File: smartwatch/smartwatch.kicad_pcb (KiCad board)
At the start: 4 copper layers, 40.1 x 40.1 mm, 33 parts, among them J1 BAT_CON, J2 DC_CON, J3 PROG_INT, J4 Screen, J5 Touch, J6 Power, J8 SD Card, SW1 SW_Push, U1 ESP32-WROVER-E, U2 MCP73831-5-OT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

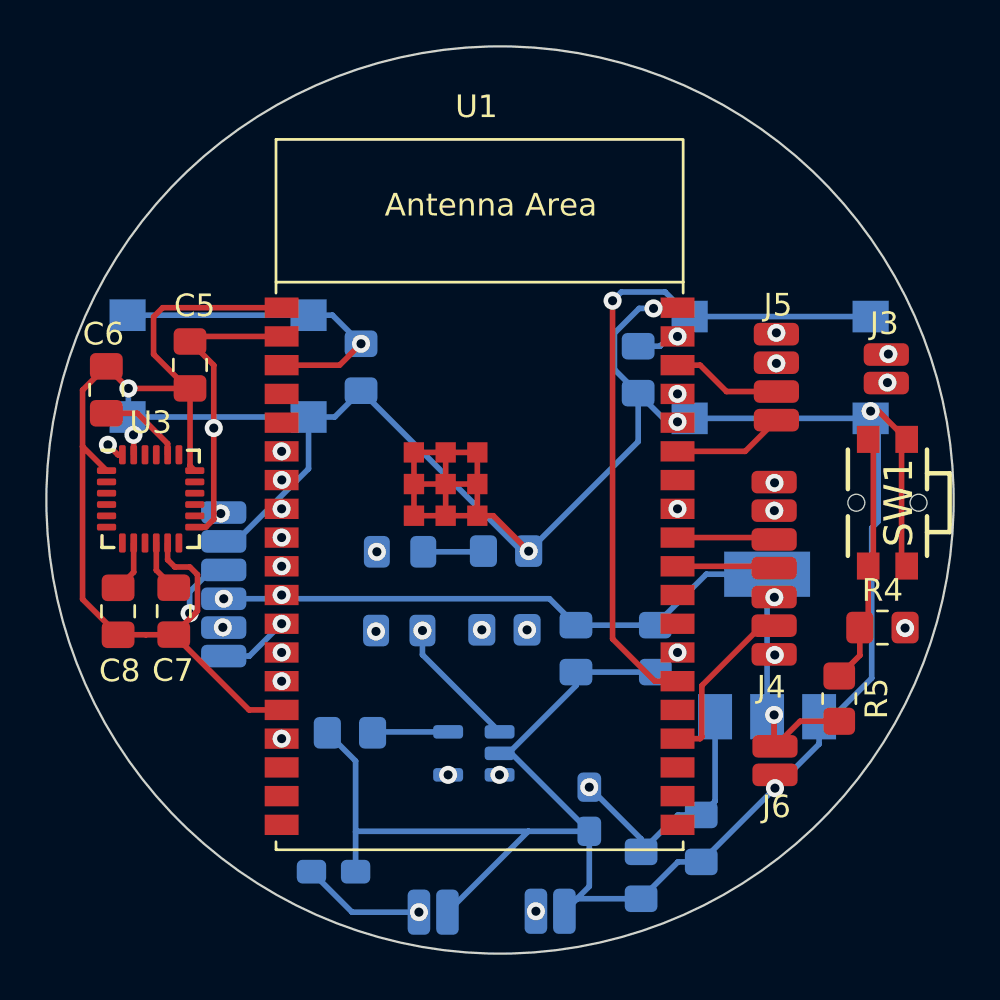
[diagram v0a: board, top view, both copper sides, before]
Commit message: fully redesigned board - ground and power planes :)
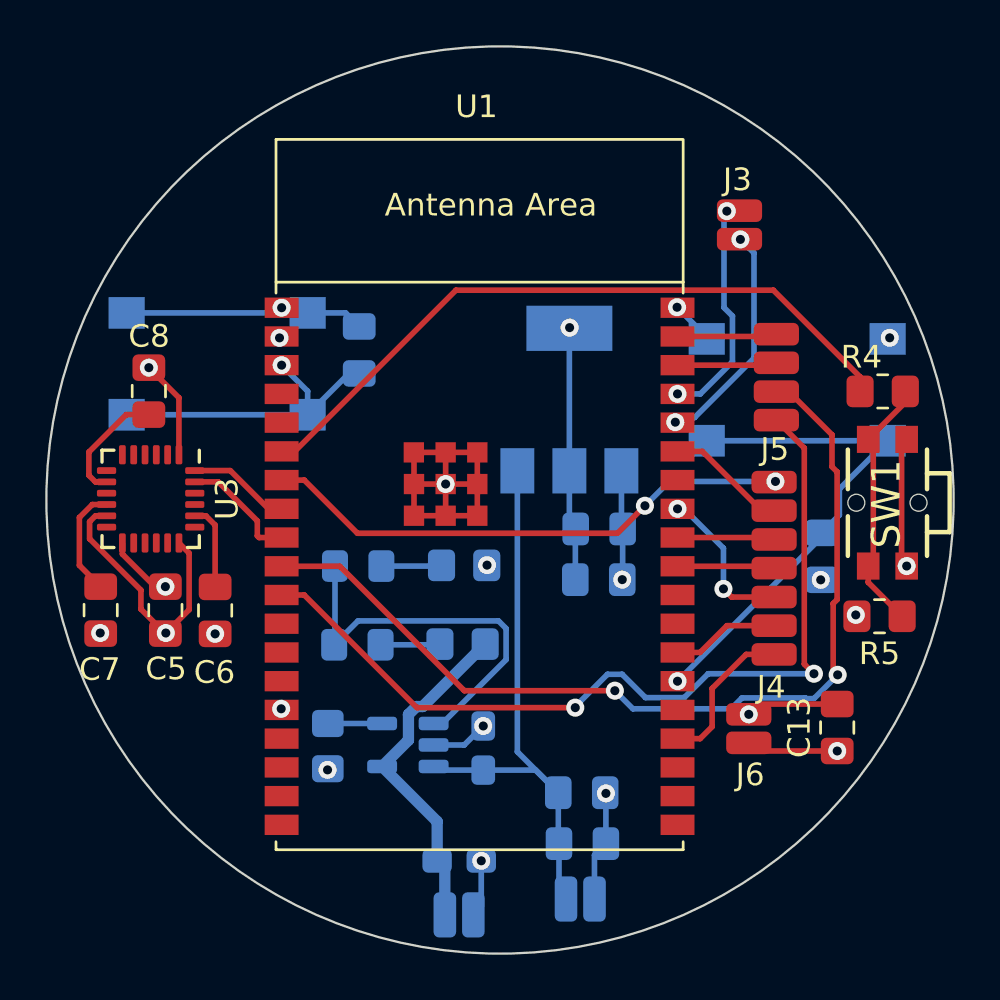
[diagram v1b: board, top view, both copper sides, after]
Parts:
- removed J8: SD Card, Connector_Wire_SMD:Wire_Pad_1x06
- added C13: 10nF, Capacitor_SMD:C_0805_2012Metric_Pad1.18x1.45mm_HandSolder, F.Cu at (60.4, 52.5)
- moved U4 13.9 mm to (48.6, 38.0)
- moved C9 11.6 mm to (59.7, 45.0)
- moved C5 10.9 mm to (30.7, 47.3)
- moved C6 10.9 mm to (32.9, 47.4), turned to -90 degrees
- moved R4 10.4 mm to (62.4, 37.7), turned to 180 degrees
- moved C8 9.83 mm to (30.0, 37.7), turned to 90 degrees
- moved J3 9.09 mm to (56.1, 30.3)
- moved C2 5.66 mm to (49.1, 55.4), turned to 180 degrees
- moved C12 5.58 mm to (43.7, 58.4)
- moved C11 5.41 mm to (44.8, 53.4), turned to 90 degrees
- moved C4 5.39 mm to (49.9, 43.8), turned to 180 degrees
- moved R5 4.05 mm to (62.3, 47.6), turned to 180 degrees
- moved C3 3.94 mm to (49.9, 46.0), turned to 180 degrees
- moved C7 3.23 mm to (27.9, 47.3)
- moved C1 2.95 mm to (49.2, 57.7), turned to 180 degrees
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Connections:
- U1 pad 12: SD_SS -> unconnected-(U1-ADC2_CH7/GPIO27-Pad12)
- U1 pad 13: SD_SCLK -> unconnected-(U1-MTMS/GPIO14/ADC2_CH6-Pad13)
- U1 pad 14: SD_MISO -> unconnected-(U1-MTDI/GPIO12/ADC2_CH5-Pad14)
- U1 pad 16: SD_MOSI -> unconnected-(U1-MTCK/GPIO13/ADC2_CH4-Pad16)
- U1 pad 23: SCR_RST -> SCR_BL
- U1 pad 24: IO2 -> unconnected-(U1-ADC2_CH2/GPIO2-Pad24)
- U1 pad 26: SCR_BL -> SCR_RST
- U1 pad 33: TOUCH_SDA -> SCR_MOSI
- U1 pad 37: SCR_MOSI -> TOUCH_SDA
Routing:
- net DC_GND: track 200.6 -> 71.8 mm, vias 5 -> 18
- net 3V3: track 57.9 -> 18.6 mm, vias 3 -> 5
- net TOUCH_IRQ: track 25.6 -> 41.9 mm, vias 3 -> 2
- net TOUCH_RST: track 27.2 -> 39.0 mm
- net IO0: track 33.4 -> 22.5 mm
- net SD_MISO: track 8.67 -> 0.00 mm, vias 2 -> 0
- net SD_SCLK: track 7.64 -> 0.00 mm, vias 2 -> 0
- net MCP_1: track 10.2 -> 17.4 mm, vias 2 -> 0
- net SD_MOSI: track 6.04 -> 0.00 mm, vias 2 -> 0
- net MPU_SDA: track 9.83 -> 4.54 mm, vias 2 -> 0
- net SCR_MOSI: track 10.0 -> 5.36 mm, vias 2 -> 0
- net BAT_VDD: track 21.5 -> 25.8 mm, vias 3 -> 0
- net Net-(RED1-A): track 6.75 -> 2.64 mm, vias 2 -> 0
- net MPU_SCL: track 9.32 -> 5.25 mm, vias 3 -> 0
- net DC_5V_IN: track 19.1 -> 15.2 mm, vias 3 -> 0
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- added copper zone on In1.Cu, net 3V3
- added copper zone on In2.Cu, net DC_GND

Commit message: implemented battery reading in both code and schem
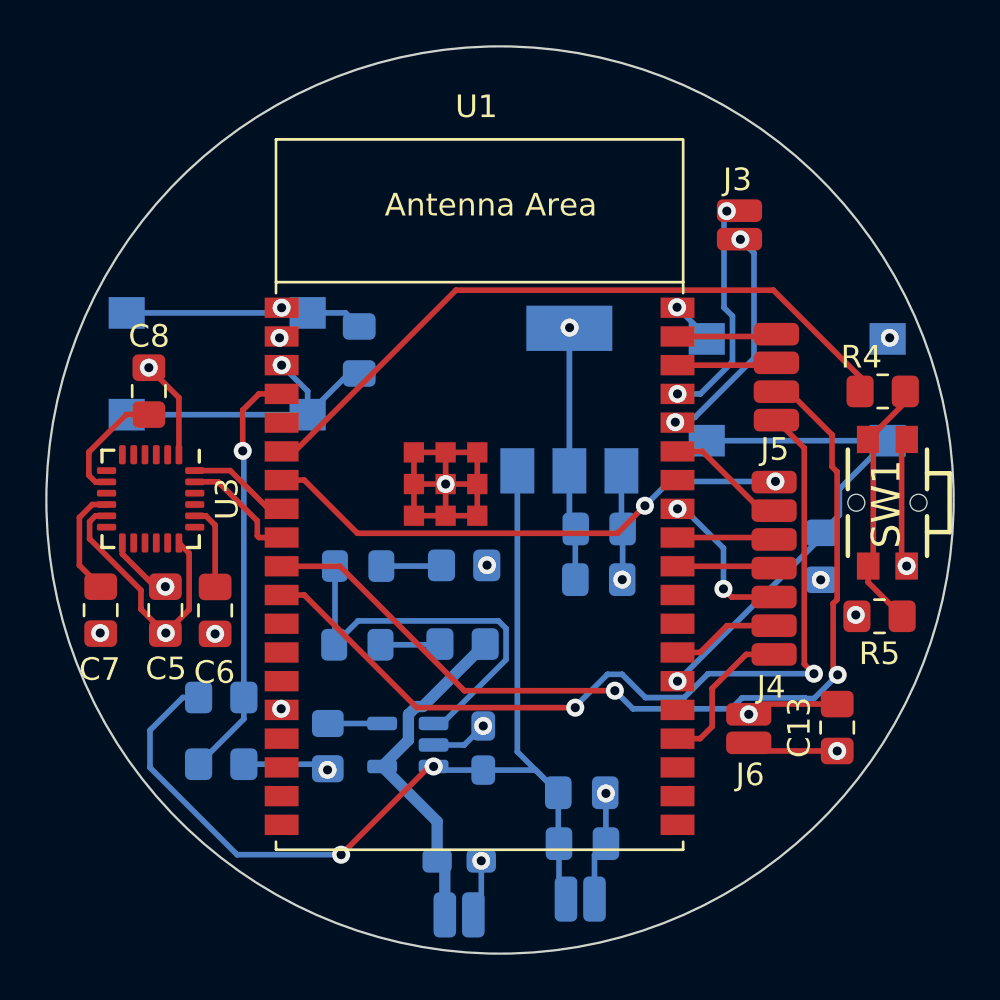
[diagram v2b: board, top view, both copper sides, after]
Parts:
- added R6: 10KΩ, Resistor_SMD:R_0805_2012Metric_Pad1.20x1.40mm_HandSolder, B.Cu at (33.2, 51.2)
- added R7: 10KΩ, Resistor_SMD:R_0805_2012Metric_Pad1.20x1.40mm_HandSolder, B.Cu at (33.2, 54.1)
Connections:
- U1 pad 4: unconnected-(U1-SENSOR_VP/GPIO36/ADC1_CH0-Pad4) -> BAT_MEASURE
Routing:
- net BAT_VDD: track 25.8 -> 46.0 mm, vias 0 -> 2
- net BAT_MEASURE: track 0.00 -> 18.5 mm, vias 0 -> 1
- net DC_GND: track 71.8 -> 75.6 mm
